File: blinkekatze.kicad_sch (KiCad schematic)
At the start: 0 parts

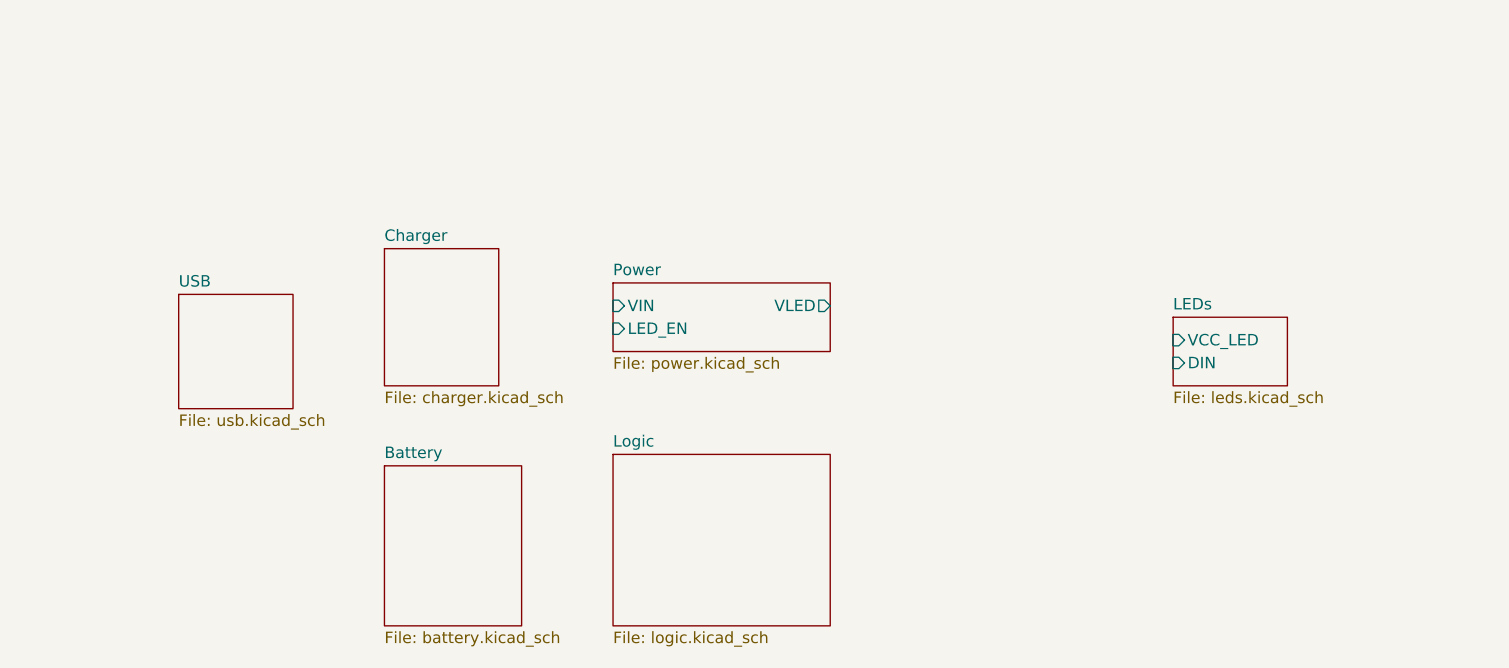
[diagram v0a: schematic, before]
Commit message: Finish preliminary charger and logic schematic
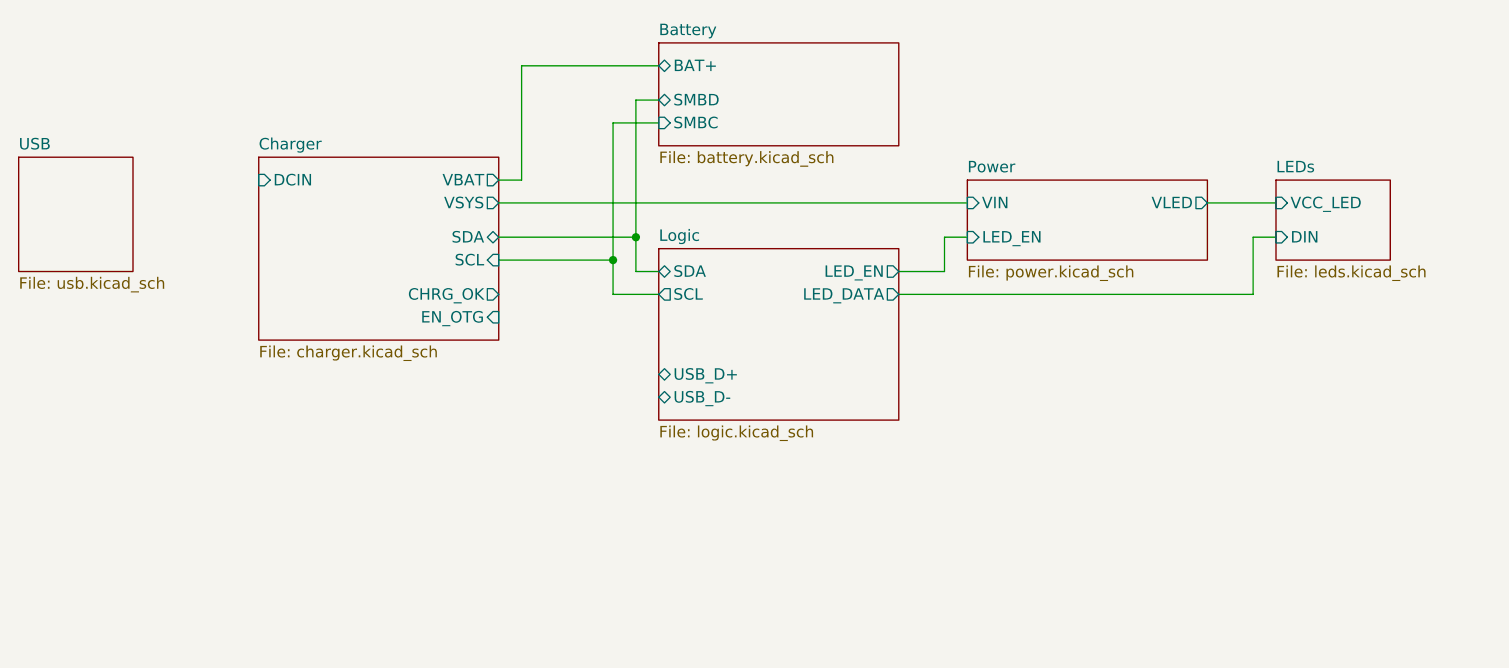
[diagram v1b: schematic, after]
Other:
- sheet Battery ports: added BAT+, SMBC, SMBD; removed none
- sheet Charger ports: added CHRG_OK, DCIN, EN_OTG, SCL, SDA, VBAT, VSYS; removed none
- sheet Logic ports: added LED_DATA, LED_EN, SCL, SDA, USB_D+, USB_D-; removed none
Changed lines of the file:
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@@
 (kicad_sch (version 20230121) (generator eeschema)
   (paper "A4")
-  (sheet (at 179.07 83.82) (size 24.13 19.05) (fields_autoplaced)
-    (stroke (width 0.1524) (type solid))
-    (fill (color 0 0 0 0.0000))
-    (property "Sheetname" "Logic" (at 179.07 83.1084 0)
-      (effects (font (size 1.27 1.27)) (justify left bottom))
-    )
-    (property "Sheetfile" "logic.kicad_sch" (at 179.07 103.4546 0)
-      (effects (font (size 1.27 1.27)) (justify left top))
+  (junction (at 179.07 62.23) (diameter 0) (color 0 0 0 0)
+  )
+  (junction (at 181.61 59.69) (diameter 0) (color 0 0 0 0)
+  )
+  (wire (pts (xy 179.07 46.99) (xy 179.07 62.23))
+    (stroke (width 0) (type default))
+  )
+  (wire (pts (xy 215.9 59.69) (xy 215.9 63.5))
+    (stroke (width 0) (type default))
+  )
+  (wire (pts (xy 166.37 55.88) (xy 218.44 55.88))
+    (stroke (width 0) (type default))
+  )
+  (wire (pts (xy 210.82 66.04) (xy 250.19 66.04))
+    (stroke (width 0) (type default))
+  )
+  (wire (pts (xy 184.15 46.99) (xy 179.07 46.99))
+    (stroke (width 0) (type default))
+  )
+  (wire (pts (xy 168.91 40.64) (xy 168.91 53.34))
+    (stroke (width 0) (type default))
+  )
+  (wire (pts (xy 181.61 44.45) (xy 184.15 44.45))
+    (stroke (width 0) (type default))
+  )
+  (wire (pts (xy 181.61 59.69) (xy 181.61 44.45))
+    (stroke (width 0) (type default))
+  )
+  (wire (pts (xy 179.07 62.23) (xy 179.07 66.04))
+    (stroke (width 0) (type default))
+  )
+  (wire (pts (xy 250.19 66.04) (xy 250.19 59.69))
+    (stroke (width 0) (type default))
+  )
+  (wire (pts (xy 168.91 53.34) (xy 166.37 53.34))
+    (stroke (width 0) (type default))
+  )
+  (wire (pts (xy 184.15 63.5) (xy 181.61 63.5))
+    (stroke (width 0) (type default))
+  )
+  (wire (pts (xy 179.07 66.04) (xy 184.15 66.04))
+    (stroke (width 0) (type default))
+  )
+  (wire (pts (xy 218.44 59.69) (xy 215.9 59.69))
+    (stroke (width 0) (type default))
+  )
+  (wire (pts (xy 215.9 63.5) (xy 210.82 63.5))
+    (stroke (width 0) (type default))
+  )
+  (wire (pts (xy 250.19 59.69) (xy 252.73 59.69))
+    (stroke (width 0) (type default))
+  )
+  (wire (pts (xy 184.15 40.64) (xy 168.91 40.64))
+    (stroke (width 0) (type default))
+  )
+  (wire (pts (xy 181.61 63.5) (xy 181.61 59.69))
+    (stroke (width 0) (type default))
+  )
+  (wire (pts (xy 166.37 59.69) (xy 181.61 59.69))
+    (stroke (width 0) (type default))
+  )
+  (wire (pts (xy 166.37 62.23) (xy 179.07 62.23))
+    (stroke (width 0) (type default))
+  )
+  (wire (pts (xy 245.11 55.88) (xy 252.73 55.88))
+    (stroke (width 0) (type default))
+  )
+  (sheet (at 184.15 60.96) (size 26.67 19.05) (fields_autoplaced)
+    (stroke (width 0.1524) (type solid))
+    (fill (color 0 0 0 0.0000))
+    (property "Sheetname" "Logic" (at 184.15 60.2484 0)
+      (effects (font (size 1.27 1.27)) (justify left bottom))
+    )
+    (property "Sheetfile" "logic.kicad_sch" (at 184.15 80.5946 0)
+      (effects (font (size 1.27 1.27)) (justify left top))
+    )
+    (pin "SCL" output (at 184.15 66.04 180)
+      (effects (font (size 1.27 1.27)) (justify left))
+    )
+    (pin "SDA" bidirectional (at 184.15 63.5 180)
+      (effects (font (size 1.27 1.27)) (justify left))
+    )
+    (pin "USB_D+" bidirectional (at 184.15 74.93 180)
+      (effects (font (size 1.27 1.27)) (justify left))
+    )
+    (pin "USB_D-" bidirectional (at 184.15 77.47 180)
+      (effects (font (size 1.27 1.27)) (justify left))
+    )
+    (pin "LED_EN" output (at 210.82 63.5 0)
+      (effects (font (size 1.27 1.27)) (justify right))
+    )
+    (pin "LED_DATA" output (at 210.82 66.04 0)
+      (effects (font (size 1.27 1.27)) (justify right))
     )
     (instances
@@
     )
   )
-  (sheet (at 153.67 85.09) (size 15.24 17.78) (fields_autoplaced)
-    (stroke (width 0.1524) (type solid))
-    (fill (color 0 0 0 0.0000))
-    (property "Sheetname" "Battery" (at 153.67 84.3784 0)
-      (effects (font (size 1.27 1.27)) (justify left bottom))
-    )
-    (property "Sheetfile" "battery.kicad_sch" (at 153.67 103.4546 0)
-      (effects (font (size 1.27 1.27)) (justify left top))
+  (sheet (at 184.15 38.1) (size 26.67 11.43) (fields_autoplaced)
+    (stroke (width 0.1524) (type solid))
+    (fill (color 0 0 0 0.0000))
+    (property "Sheetname" "Battery" (at 184.15 37.3884 0)
+      (effects (font (size 1.27 1.27)) (justify left bottom))
+    )
+    (property "Sheetfile" "battery.kicad_sch" (at 184.15 50.1146 0)
+      (effects (font (size 1.27 1.27)) (justify left top))
+    )
+    (pin "BAT+" bidirectional (at 184.15 40.64 180)
+      (effects (font (size 1.27 1.27)) (justify left))
+    )
+    (pin "SMBC" input (at 184.15 46.99 180)
+      (effects (font (size 1.27 1.27)) (justify left))
+    )
+    (pin "SMBD" bidirectional (at 184.15 44.45 180)
+      (effects (font (size 1.27 1.27)) (justify left))
     )
     (instances
@@
     )
   )
-  (sheet (at 241.3 68.58) (size 12.7 7.62) (fields_autoplaced)
-    (stroke (width 0.1524) (type solid))
-    (fill (color 0 0 0 0.0000))
-    (property "Sheetname" "LEDs" (at 241.3 67.8684 0)
-      (effects (font (size 1.27 1.27)) (justify left bottom))
-    )
-    (property "Sheetfile" "leds.kicad_sch" (at 241.3 76.7846 0)
-      (effects (font (size 1.27 1.27)) (justify left top))
-    )
-    (pin "DIN" input (at 241.3 73.66 180)
-      (effects (font (size 1.27 1.27)) (justify left))
-    )
-    (pin "VCC_LED" input (at 241.3 71.12 180)
+  (sheet (at 252.73 53.34) (size 12.7 8.89) (fields_autoplaced)
+    (stroke (width 0.1524) (type solid))
+    (fill (color 0 0 0 0.0000))
+    (property "Sheetname" "LEDs" (at 252.73 52.6284 0)
+      (effects (font (size 1.27 1.27)) (justify left bottom))
+    )
+    (property "Sheetfile" "leds.kicad_sch" (at 252.73 62.8146 0)
+      (effects (font (size 1.27 1.27)) (justify left top))
+    )
+    (pin "DIN" input (at 252.73 59.69 180)
+      (effects (font (size 1.27 1.27)) (justify left))
+    )
+    (pin "VCC_LED" input (at 252.73 55.88 180)
       (effects (font (size 1.27 1.27)) (justify left))
     )
@@
     )
   )
-  (sheet (at 130.81 66.04) (size 12.7 12.7) (fields_autoplaced)
-    (stroke (width 0.1524) (type solid))
-    (fill (color 0 0 0 0.0000))
-    (property "Sheetname" "USB" (at 130.81 65.3284 0)
-      (effects (font (size 1.27 1.27)) (justify left bottom))
-    )
-    (property "Sheetfile" "usb.kicad_sch" (at 130.81 79.3246 0)
+  (sheet (at 113.03 50.8) (size 12.7 12.7) (fields_autoplaced)
+    (stroke (width 0.1524) (type solid))
+    (fill (color 0 0 0 0.0000))
+    (property "Sheetname" "USB" (at 113.03 50.0884 0)
+      (effects (font (size 1.27 1.27)) (justify left bottom))
+    )
+    (property "Sheetfile" "usb.kicad_sch" (at 113.03 64.0846 0)
       (effects (font (size 1.27 1.27)) (justify left top))
     )
@@
     )
   )
-  (sheet (at 153.67 60.96) (size 12.7 15.24) (fields_autoplaced)
-    (stroke (width 0.1524) (type solid))
-    (fill (color 0 0 0 0.0000))
-    (property "Sheetname" "Charger" (at 153.67 60.2484 0)
-      (effects (font (size 1.27 1.27)) (justify left bottom))
-    )
-    (property "Sheetfile" "charger.kicad_sch" (at 153.67 76.7846 0)
-      (effects (font (size 1.27 1.27)) (justify left top))
+  (sheet (at 139.7 50.8) (size 26.67 20.32) (fields_autoplaced)
+    (stroke (width 0.1524) (type solid))
+    (fill (color 0 0 0 0.0000))
+    (property "Sheetname" "Charger" (at 139.7 50.0884 0)
+      (effects (font (size 1.27 1.27)) (justify left bottom))
+    )
+    (property "Sheetfile" "charger.kicad_sch" (at 139.7 71.7046 0)
+      (effects (font (size 1.27 1.27)) (justify left top))
+    )
+    (pin "DCIN" input (at 139.7 53.34 180)
+      (effects (font (size 1.27 1.27)) (justify left))
+    )
+    (pin "VSYS" output (at 166.37 55.88 0)
+      (effects (font (size 1.27 1.27)) (justify right))
+    )
+    (pin "VBAT" output (at 166.37 53.34 0)
+      (effects (font (size 1.27 1.27)) (justify right))
+    )
+    (pin "SDA" bidirectional (at 166.37 59.69 0)
+      (effects (font (size 1.27 1.27)) (justify right))
+    )
+    (pin "CHRG_OK" output (at 166.37 66.04 0)
+      (effects (font (size 1.27 1.27)) (justify right))
+    )
+    (pin "EN_OTG" input (at 166.37 68.58 0)
+      (effects (font (size 1.27 1.27)) (justify right))
+    )
+    (pin "SCL" input (at 166.37 62.23 0)
+      (effects (font (size 1.27 1.27)) (justify right))
     )
     (instances
@@
     )
   )
-  (sheet (at 179.07 64.77) (size 24.13 7.62) (fields_autoplaced)
-    (stroke (width 0.1524) (type solid))
-    (fill (color 0 0 0 0.0000))
-    (property "Sheetname" "Power" (at 179.07 64.0584 0)
-      (effects (font (size 1.27 1.27)) (justify left bottom))
-    )
-    (property "Sheetfile" "power.kicad_sch" (at 179.07 72.9746 0)
-      (effects (font (size 1.27 1.27)) (justify left top))
-    )
-    (pin "VLED" output (at 203.2 67.31 0)
-      (effects (font (size 1.27 1.27)) (justify right))
-    )
-    (pin "VIN" input (at 179.07 67.31 180)
-      (effects (font (size 1.27 1.27)) (justify left))
-    )
-    (pin "LED_EN" input (at 179.07 69.85 180)
-      (effects (font (size 1.27 1.27)) (justify left))
-    )
+  (sheet (at 218.44 53.34) (size 26.67 8.89) (fields_autoplaced)
+    (stroke (width 0.1524) (type solid))
+    (fill (color 0 0 0 0.0000))
+    (property "Sheetname" "Power" (at 218.44 52.6284 0)
+      (effects (font (size 1.27 1.27)) (justify left bottom))
+    )
+    (property "Sheetfile" "power.kicad_sch" (at 218.44 62.8146 0)
+      (effects (font (size 1.27 1.27)) (justify left top))
+    )
+    (pin "VLED" output (at 245.11 55.88 0)
+      (effects (font (size 1.27 1.27)) (justify right))
+    )
+    (pin "VIN" input (at 218.44 55.88 180)
+      (effects (font (size 1.27 1.27)) (justify left))
+    )
+    (pin "LED_EN" input (at 218.44 59.69 180)
+      (effects (font (size 1.27 1.27)) (justify left))
+    )

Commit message: Aesthetic top level schematic fixes
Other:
- sheet USB ports: added VUSB; removed none

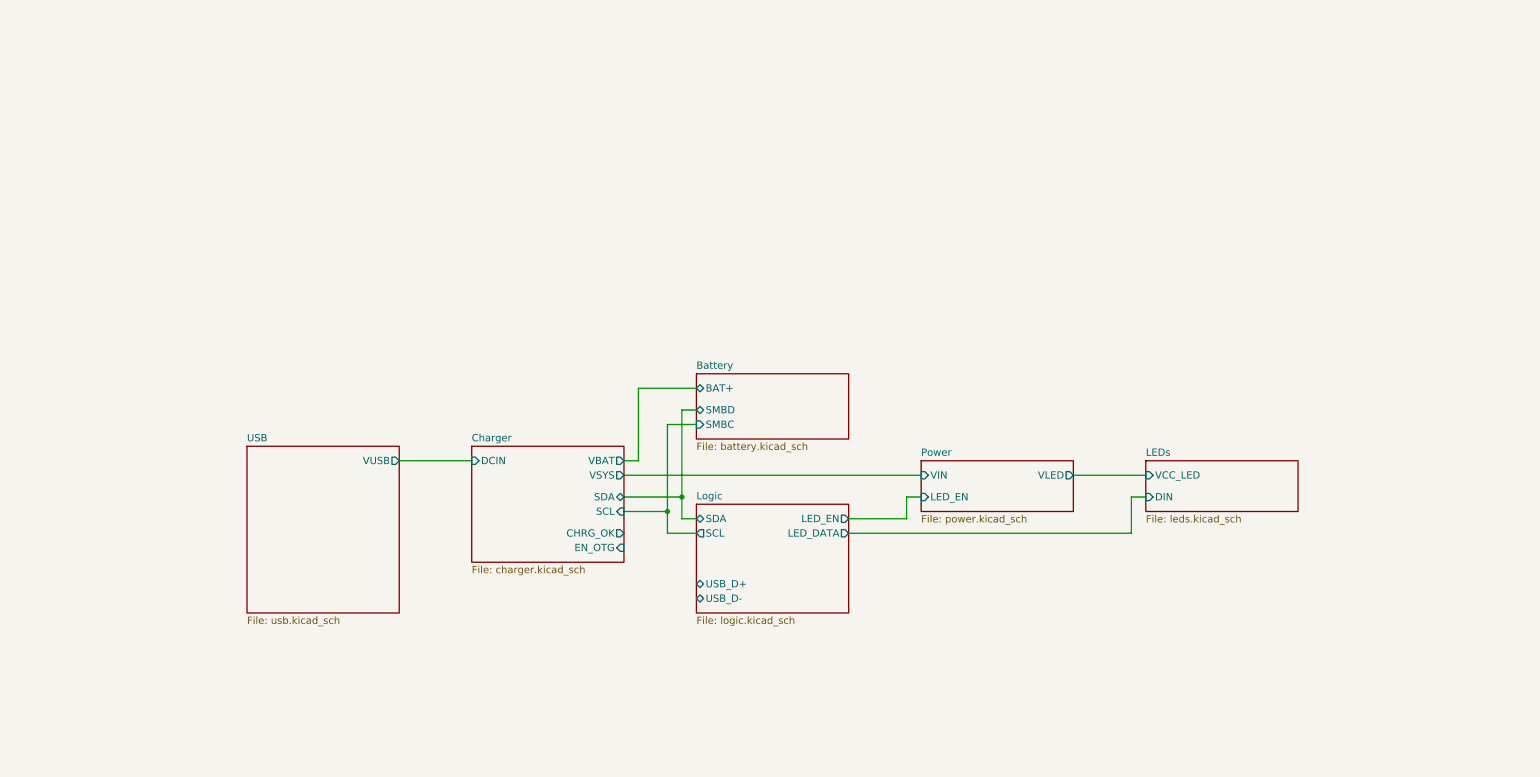
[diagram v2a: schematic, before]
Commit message: Finish rough layout
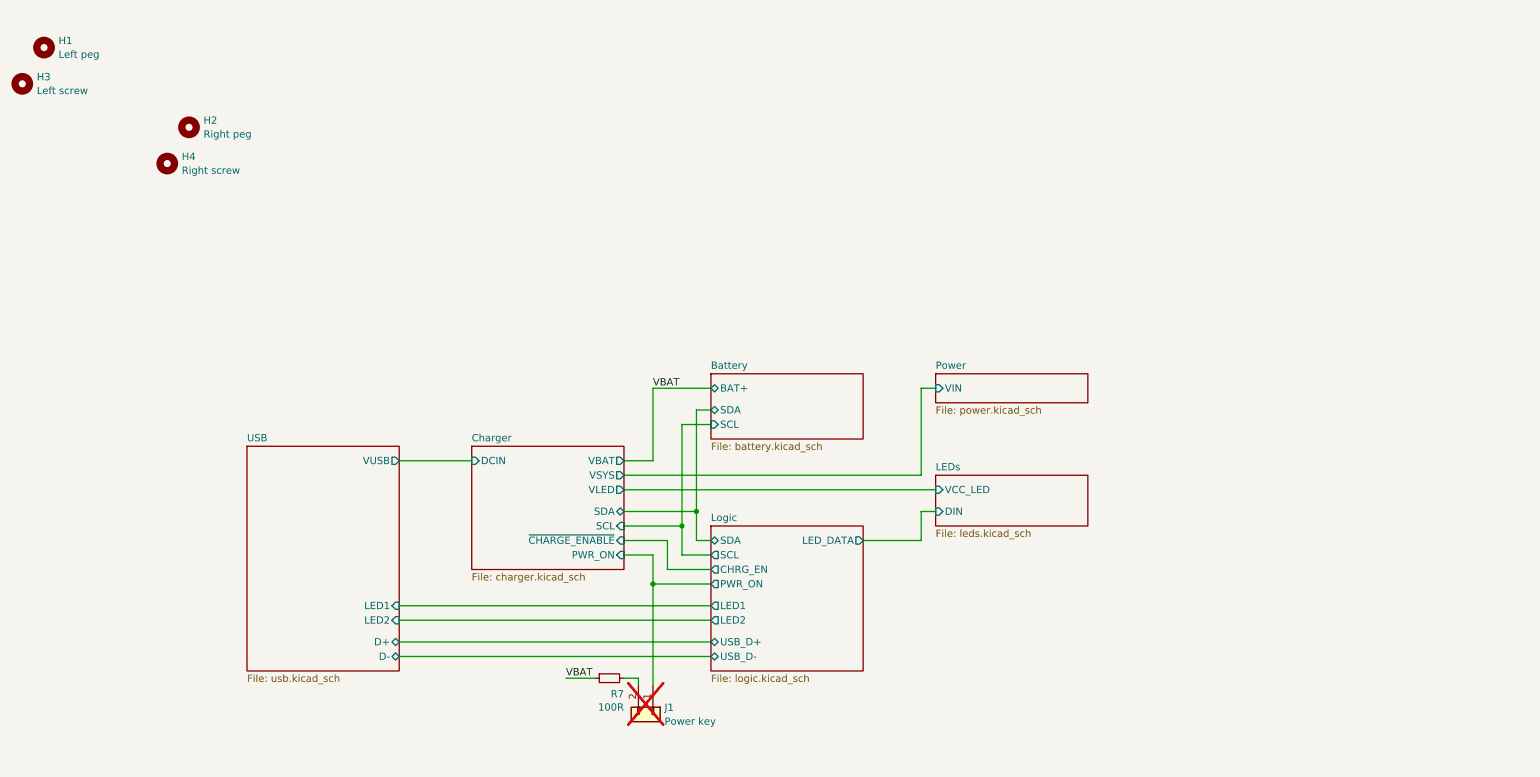
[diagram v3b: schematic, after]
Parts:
- added H1: Left peg, MountingHole:MountingHole_2.1mm, symbol Mechanical:MountingHole
- added H2: Right peg, MountingHole:MountingHole_2.1mm, symbol Mechanical:MountingHole
- added H3: Left screw, MountingHole:MountingHole_2.5mm, symbol Mechanical:MountingHole
- added H4: Right screw, MountingHole:MountingHole_2.5mm, symbol Mechanical:MountingHole
- added J1: Power key, Connector_PinHeader_2.54mm:PinHeader_1x02_P2.54mm_Vertical, symbol Connector_Generic:Conn_01x02
- added R7: 100R, Resistor_SMD:R_0402_1005Metric, symbol Device:R_Small
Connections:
- new net: J1.2 (Pin_2), R7.2
- new net Charger/PWR_ON: J1.1 (Pin_1)
- new net VBAT: R7.1
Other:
- sheet Battery ports: added SCL, SDA; removed SMBC, SMBD
- sheet Charger ports: added PWR_ON, VLED, ~{CHARGE_ENABLE}; removed CHRG_OK, EN_OTG
- sheet Logic ports: added CHRG_EN, LED1, LED2, PWR_ON; removed LED_EN
- sheet Power ports: added none; removed LED_EN, VLED
- sheet USB ports: added D+, D-, LED1, LED2; removed none

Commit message: JLCPCB DFM
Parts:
- added H5, H6: Tooling hole, ToolingHole:ToolingHole_JLCSMT, symbol Mechanical:MountingHole
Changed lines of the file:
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@@
+    )
+  )
+  (symbol (lib_id "Mechanical:MountingHole") (at 267.97 21.59 0) (unit 1)
+    (in_bom no) (on_board yes) (dnp no) (fields_autoplaced)
+    (property "Reference" "H6" (at 270.51 20.3779 0)
+      (effects (font (size 1.27 1.27)) (justify left))
+    )
+    (property "Value" "Tooling hole" (at 270.51 22.8021 0)
+      (effects (font (size 1.27 1.27)) (justify left))
+    )
+    (property "Footprint" "ToolingHole:ToolingHole_JLCSMT" (at 267.97 21.59 0)
+      (effects (font (size 1.27 1.27)) hide)
+    )
+    (property "Datasheet" "~" (at 267.97 21.59 0)
+      (effects (font (size 1.27 1.27)) hide)
+    )
+    (instances
+      (project "blinkekatze"
+        (path "/20b2a5b0-0a80-4b97-84d4-d5290b2926e5"
+          (reference "H6") (unit 1)
+        )
+      )
     )
   )
@@
         )
       )
+    )
+  )
+  (symbol (lib_id "Mechanical:MountingHole") (at 267.97 16.51 0) (unit 1)
+    (in_bom no) (on_board yes) (dnp no) (fields_autoplaced)
+    (property "Reference" "H5" (at 270.51 15.2979 0)
+      (effects (font (size 1.27 1.27)) (justify left))
+    )
+    (property "Value" "Tooling hole" (at 270.51 17.7221 0)
+      (effects (font (size 1.27 1.27)) (justify left))
+    )
+    (property "Footprint" "ToolingHole:ToolingHole_JLCSMT" (at 267.97 16.51 0)
+      (effects (font (size 1.27 1.27)) hide)
+    )
+    (property "Datasheet" "~" (at 267.97 16.51 0)
+      (effects (font (size 1.27 1.27)) hide)
+    )
+    (instances
+      (project "blinkekatze"
+        (path "/20b2a5b0-0a80-4b97-84d4-d5290b2926e5"
+          (reference "H5") (unit 1)
+        )
+      )

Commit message: Add accelerometer
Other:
- note added: "I2C Addresses ================ 0x18 LIS3D 0x29 303ALS-01 0x55 BQ27546 0x6B BQ24295"
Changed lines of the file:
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@@
     (stroke (width 0) (type default))
+  )
+  (text "I2C Addresses\n================\n0x18   LIS3D\n0x29   303ALS-01\n0x55   BQ27546\n0x6B   BQ24295\n"
+    (at 85.09 33.02 0)
+    (effects (font (face "Droid Sans Mono") (size 1.27 1.27)) (justify left bottom))
   )
   (label "VBAT" (at 116.84 130.81 0) (fields_autoplaced)
